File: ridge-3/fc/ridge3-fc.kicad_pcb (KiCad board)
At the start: 6 copper layers, 36 x 36 mm, 119 parts, among them Y1 8MHz, Y2 27MHz

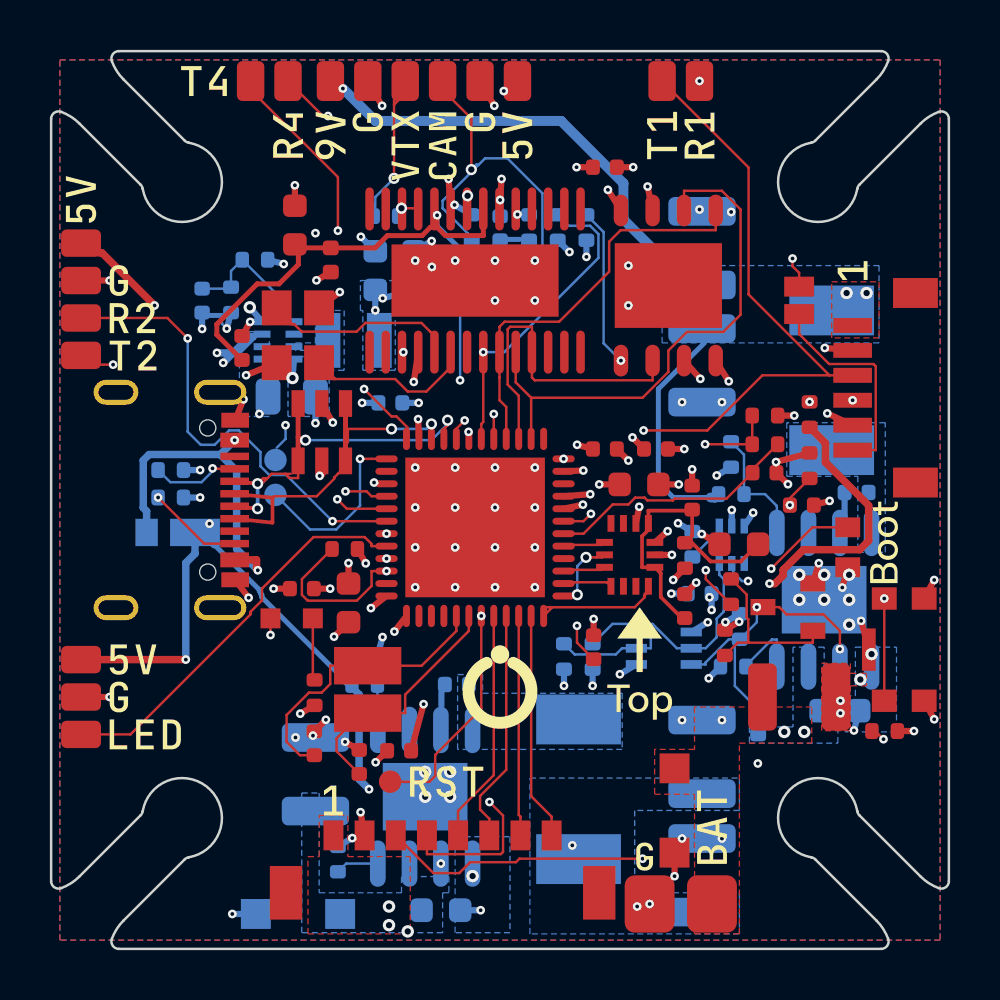
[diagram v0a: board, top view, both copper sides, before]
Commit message: FC rebuilt with +3V3 on the stack lead's pin 4; name placed with room for the flag
The FC routed to DRC 0 with J_ESC pin 4 on +3V3 (the ESC's MCUs) and PB11
unconnected; all gates pass (92 assembled parts).

Silkscreen: the product name took the spot with the fewest vias under it,
which can leave the flag over it 0.06 mm short of room (a part's pads above).
The name now takes only a spot that leaves the flag room above it
(SilkPlacer.text's accept, SilkPlacer.fits).

Co-Authored-By: Claude Opus 5.5 <noreply@anthropic.com>
Claude-Session: https://claude.ai/code/session_01MaVFAzoExts7u2gmCraXFC
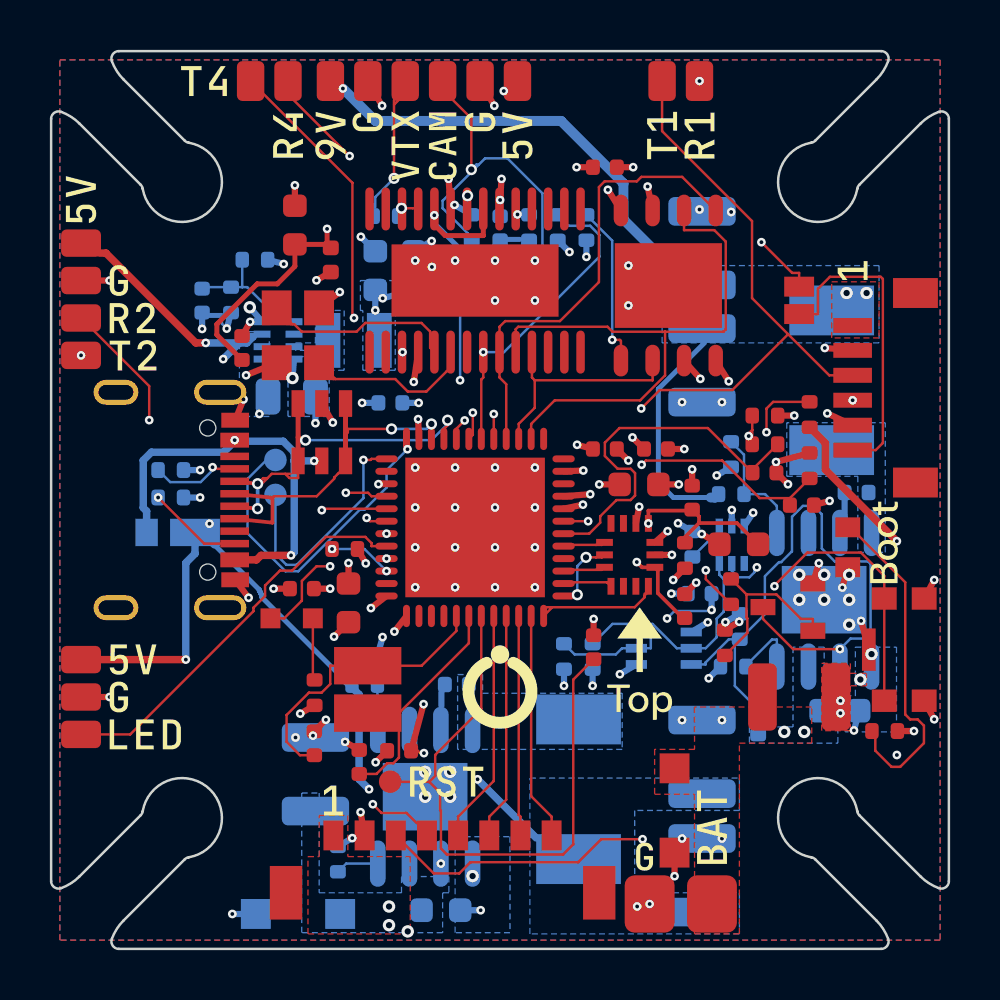
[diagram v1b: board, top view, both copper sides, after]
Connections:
- J_ESC pad 4: TLM -> +3V3
- U_FC pad 24: TLM -> (no net)
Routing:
- net TLM: track 21.2 -> 0.00 mm, vias 2 -> 0
- net BUCK9_EN: track 12.4 -> 25.7 mm, vias 2 -> 1
- net NRST: track 14.7 -> 25.3 mm, vias 2 -> 0
- net +3V3: track 29.7 -> 40.1 mm, vias 34 -> 36
- net SWDIO: track 7.19 -> 13.5 mm, vias 2 -> 1
- net ADC_VBAT: track 15.4 -> 20.5 mm
- net ADC_CURR: track 10.2 -> 15.0 mm
- net SPI2_MISO: track 13.3 -> 9.31 mm
- net HD_SBUS: track 8.70 -> 12.5 mm
- net UART2_RX: track 45.4 -> 41.8 mm
- net BOOT0: track 32.2 -> 29.3 mm, vias 2 -> 3
- net SPI2_SCK: track 21.6 -> 24.2 mm
- net VBAT: track 32.1 -> 34.7 mm
- net SWCLK: track 7.30 -> 9.66 mm
- net SPI2_MOSI: track 16.4 -> 18.6 mm
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
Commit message: FC: HD video on solder pads, the analog OSD as its own build
The JST-SH HD port (an 85 C part with no hotter SH-compatible header)
passed its rating within minutes on the ground in still air.  The air unit
now solders to four pads on the front edge (9V G T1 R1, MSP DisplayPort on
UART1); SBUS, where an air unit carries it, goes to R2 in place of the
receiver's TX, so the SBUS jumper goes too.

The option groups are now video (the 9 V supply, its switch and
thermostat, the video pads), analog (the AT7456E OSD, its parts, the
camera and analog VTX pads) and blackbox.  circuit.BUILDS names what each
build fits: 'hd', the default, leaves the analog OSD off; 'analog' fits it.
make.py writes the default build's BOM and CPL and the analog build's
beside them (-analog), and gates both.  The stack model and the stress
report follow the build (the OSD, and rev 1's HD socket, only where
fitted).

Placed and routed again from scratch: DRC 0/0/0, copper equal to
circuit.py pad for pad.

Co-Authored-By: Claude Opus 5.5 <noreply@anthropic.com>
Claude-Session: https://claude.ai/code/session_01MaVFAzoExts7u2gmCraXFC
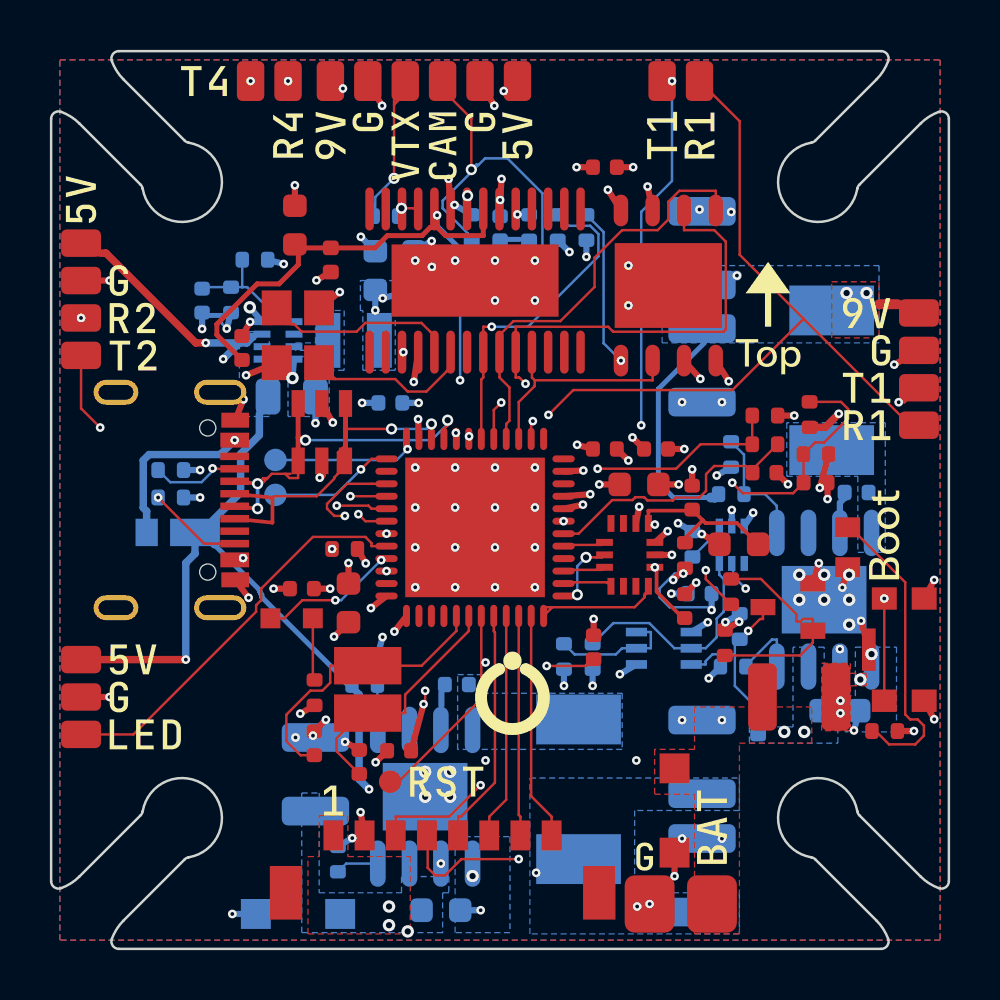
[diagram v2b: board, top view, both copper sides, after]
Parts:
- removed J_HD: SH-6P V, CONN-SMD-6P-P1.00_BM06B-SRSS-TB-LF-SN
- removed SJ_SBUS: SJ_OPEN, SJ_OPEN
- added P_HD9V: PAD_SIG, PAD_SIG, F.Cu at (116.8, 92.5)
- added P_HDG: PAD_SIG, PAD_SIG, F.Cu at (116.8, 94.0)
- added P_HDR: PAD_SIG, PAD_SIG, F.Cu at (116.8, 97.0)
- added P_HDT: PAD_SIG, PAD_SIG, F.Cu at (116.8, 95.5)
- moved C2 1.05 mm to (112.7, 99.3)
- moved R4 0.53 mm to (112.7, 98.2), turned to 0 degrees
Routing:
- net UART2_RX: track 41.8 -> 15.8 mm, vias 3 -> 2
- net BUCK9_EN: track 25.7 -> 11.7 mm, vias 1 -> 2
- net HD_SBUS: track 12.5 -> 0.00 mm
- net NRST: track 25.3 -> 13.0 mm, vias 0 -> 2
- net +3V3: track 40.1 -> 48.3 mm
- net SWDIO: track 13.5 -> 5.91 mm
- net VBAT: track 34.7 -> 29.6 mm, vias 6 -> 7
- net SWCLK: track 9.66 -> 5.05 mm
- net SPI2_SCK: track 24.2 -> 19.6 mm, vias 0 -> 2
- net ADC_VBAT: track 20.5 -> 16.2 mm, vias 3 -> 2
- net ADC_CURR: track 15.0 -> 10.9 mm
- net UART4_TX: track 18.6 -> 22.8 mm
- net CUR: track 30.5 -> 27.1 mm
- net UART1_TX: track 30.9 -> 33.7 mm, vias 2 -> 4
- net +9V: track 26.2 -> 28.8 mm, vias 3 -> 4
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
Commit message: Ridge 3 FC: placed and routed again with D10-D12; outputs, panel and VERIFICATION.md
KiCad DRC 0 / 0 / 0; every make.py gate passes; verify.py 260 passed, 0
failed with every source set (214 passed, 29 SKIP without them).  The
three supply feedback lines each reach one pour and no load's pad.

Co-Authored-By: Claude Opus 5.5 <noreply@anthropic.com>
Claude-Session: https://claude.ai/code/session_01MaVFAzoExts7u2gmCraXFC
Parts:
- added C37: 100nF, C_0402_1005Metric, B.Cu at (98.4, 91.8)
- added R31: 1k, R_0402_1005Metric, F.Cu at (115.4, 109.3)
- added R32: 330R, R_0402_1005Metric, F.Cu at (92.6, 107.7)
- C17: value 10pF -> 10uF; footprint C_0402_1005Metric -> C_0805_2012Metric
- C18: value 100nF -> 10pF; moved to B.Cu
- C20, C34, R6, R7: moved to F.Cu
- C21: moved to B.Cu
- C23: value 1uF -> 100nF; footprint C_0603_1608Metric -> C_0402_1005Metric
- C24: value 4.7uF -> 1uF
- C25, C29, C33: value 100nF -> 4.7uF; footprint C_0402_1005Metric -> C_0603_1608Metric
- C26: value 10pF -> 100nF
- C28: value 4.7uF -> 10pF; footprint C_0603_1608Metric -> C_0402_1005Metric
- C32: value 4.7uF -> 100nF; footprint C_0603_1608Metric -> C_0402_1005Metric
- R10: value 24.9k -> 57.6k
- R11: value 100R -> 100k; moved to B.Cu
- R12: value 100k -> 24.9k; moved to B.Cu
- R13: value 121k -> 100R; moved to F.Cu
- R14: value 10k -> 100k; moved to F.Cu
- R15: value 100k -> 121k
- R16: value 100k -> 10k
- R17: value 12.4k -> 100k
- R19: value 22.1k -> 12.4k
- R20: value 3.3k -> 100k; moved to B.Cu
- R21: value 10R -> 22.1k; moved to B.Cu
- R22: value 10k -> 3.3k; moved to F.Cu
- R23: value 10k -> 10R; moved to F.Cu
- R25, R26: value 75R -> 10k
- R27, R28: value 5.1k -> 75R
- R29: value 1k -> 5.1k; moved to B.Cu
- R30: value 330R -> 5.1k; moved to B.Cu
- R8: value 57.6k -> 100k
- R9: value 100k -> 24.9k
- moved R29 30.5 mm to (86.8, 98.8), turned to 0 degrees
- moved R18 21.5 mm to (109.3, 99.8), turned to 0 degrees
- moved R21 20.9 mm to (90.2, 90.4), turned to 0 degrees
- moved R19 20.6 mm to (109.3, 98.2), turned to -90 degrees
- moved C18 19.7 mm to (88.1, 92.0), turned to 90 degrees
- moved C28 17.5 mm to (94.4, 110.5), turned to 90 degrees
- moved R22 16.1 mm to (93.8, 102.0), turned to 0 degrees
- moved R9 16.0 mm to (94.6, 106.3), turned to 0 degrees
- moved R27 15.5 mm to (98.9, 89.1), turned to 90 degrees
- moved C22 15.3 mm to (92.1, 103.6)
- moved R8 14.8 mm to (94.6, 107.4), turned to 0 degrees
- moved C19 14.6 mm to (96.0, 110.1), turned to 180 degrees
- moved R28 14.2 mm to (95.4, 88.6), turned to 180 degrees
- moved R23 14.1 mm to (107.4, 102.2)
- moved C31 13.7 mm to (107.7, 99.9), turned to 90 degrees
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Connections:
- C17 pad 2: BUCK3_FB -> GND
- C18 pad 2: GND -> BUCK3_FB
- C25 pad 1: NRST -> +3V3
- C26 pad 1: HSE_IN -> NRST
- C27 pad 1: HSE_OUT -> HSE_IN
- C28 pad 1: +3V3_GYRO -> HSE_OUT
- C31 pad 1: +3V3 -> +3V3_GYRO
- C32 pad 1: +3V3_OSD -> +3V3
- C36 pad 1: CAM_VIDEO -> +3V3_OSD
- C36 pad 2: OSD_VIN -> GND
- R10 pad 1: BUCK9_EN -> BUCK9_RT
- R11 pad 1: VTX_OFF -> VBAT_VTX
- R11 pad 2: VTX_OFF_G -> BUCK9_EN
- R12 pad 1: VTX_OFF_G -> BUCK9_EN
- R13 pad 1: VTX_TSET -> VTX_OFF
- R13 pad 2: GND -> VTX_OFF_G
- R14 pad 1: +3V3 -> VTX_OFF_G
- R14 pad 2: VTX_COOL -> GND
- R15 pad 1: +3V3 -> VTX_TSET
- R15 pad 2: VTX_HOT_G -> GND
- R16 pad 1: +9V -> +3V3
- R16 pad 2: BUCK9_FB -> VTX_COOL
- R17 pad 1: BUCK9_FB -> +3V3
- R17 pad 2: GND -> VTX_HOT_G
- R18 pad 1: +3V3 -> +9V
- R18 pad 2: BUCK3_FB -> BUCK9_FB
- R19 pad 1: BUCK3_FB -> BUCK9_FB
- R20 pad 1: BOOT0 -> +3V3
- R20 pad 2: GND -> BUCK3_FB
- R21 pad 1: +3V3 -> BUCK3_FB
- R21 pad 2: +3V3_GYRO -> GND
- R22 pad 1: +3V3 -> BOOT0
- R22 pad 2: FLASH_CS -> GND
- R23 pad 2: OSD_CS -> +3V3_GYRO
- R24 pad 1: +3V3_OSD -> +3V3
- R24 pad 2: OSD_RST -> FLASH_CS
- R25 pad 1: CAM_VIDEO -> +3V3
- R25 pad 2: GND -> OSD_CS
- R26 pad 1: OSD_VOUT -> +3V3_OSD
- R26 pad 2: VTX_VIDEO -> OSD_RST
- R27 pad 1: USB_CC1 -> CAM_VIDEO
- R28 pad 1: USB_CC2 -> OSD_VOUT
- R28 pad 2: GND -> VTX_VIDEO
- R29 pad 1: +3V3 -> USB_CC1
- R29 pad 2: LED_PWR_A -> GND
- R30 pad 1: +3V3 -> USB_CC2
- R30 pad 2: LED0_A -> GND
- R6 pad 1: +5V -> VBAT
- R6 pad 2: BUCK5_FB -> BUCK5_EN
- R7 pad 1: BUCK5_FB -> BUCK5_EN
- R8 pad 1: BUCK9_RT -> +5V
- R8 pad 2: GND -> BUCK5_FB
- R9 pad 1: VBAT_VTX -> BUCK5_FB
- R9 pad 2: BUCK9_EN -> GND
- U_BUCK5 pad 2: VBAT -> BUCK5_EN
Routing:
- net +5V: track 62.1 -> 93.1 mm, vias 6 -> 9
- net BUCK5_EN: track 0.00 -> 11.5 mm, vias 0 -> 1
- net VBAT: track 29.6 -> 37.7 mm, vias 7 -> 6
- net M4_SIG: track 9.14 -> 14.5 mm
- net UART1_TX: track 33.7 -> 39.0 mm, vias 4 -> 3
- net UART4_TX: track 22.8 -> 18.9 mm
- net VTX_OFF: track 15.2 -> 18.4 mm
- net SPI2_MISO: track 9.31 -> 12.5 mm
- net +3V3: track 48.3 -> 51.2 mm, vias 36 -> 34
- net CUR: track 27.1 -> 29.9 mm
- net GND: track 60.7 -> 62.5 mm, vias 121 -> 123
- net +3V3_GYRO: track 11.3 -> 13.1 mm, vias 2 -> 0
- net SPI2_SCK: track 19.6 -> 21.3 mm, vias 2 -> 0
- net +9V: track 28.8 -> 27.2 mm, vias 4 -> 3
- net USB_VBUS: track 16.9 -> 15.6 mm
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
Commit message: Ridge 3 FC: power vias on the 2 A supplies, routed again
Every via the routers put on +5V, +9V and VBAT_VTX is now 0.5 / 0.25 mm
(fc_layout.VIA_BY_NET, honoured by Freerouting through the netclass and
by the in-house routers per net).  The first reroute took the 5 V rail's
2 A through one 0.15 mm signal via; now every via on the rail is a power
via.  verify.py checks it: 263 passed, 0 failed with every source (217,
29 SKIP without them).  DRC 0 / 0 / 0, every make.py gate.

Co-Authored-By: Claude Opus 5.5 <noreply@anthropic.com>
Claude-Session: https://claude.ai/code/session_01MaVFAzoExts7u2gmCraXFC
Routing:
- net +5V: track 93.1 -> 100.7 mm, vias 9 -> 7
- net GND: vias 123 -> 122
